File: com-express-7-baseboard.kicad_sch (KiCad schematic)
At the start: 0 parts

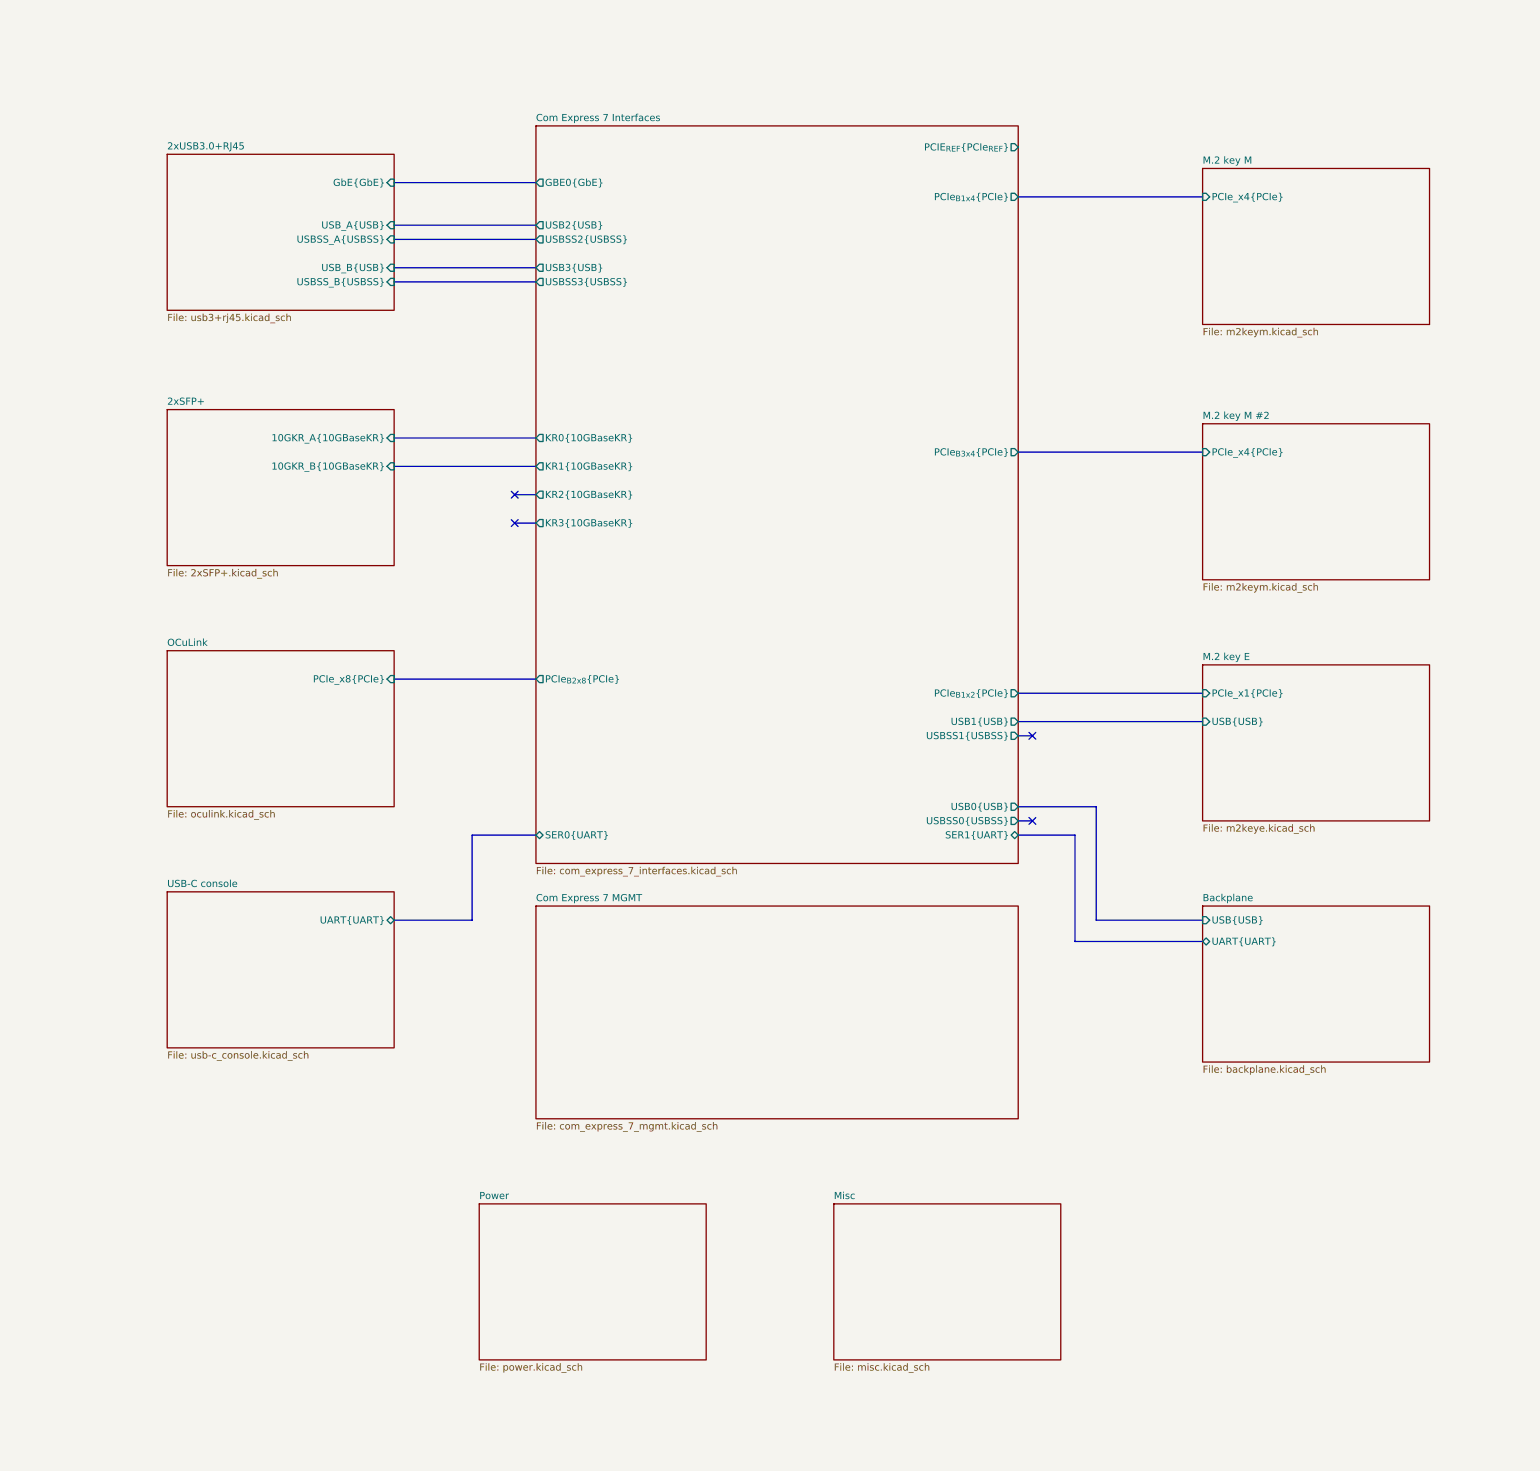
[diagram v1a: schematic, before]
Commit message: [#57056] Create schematics for M.2 and OCuLink connectors
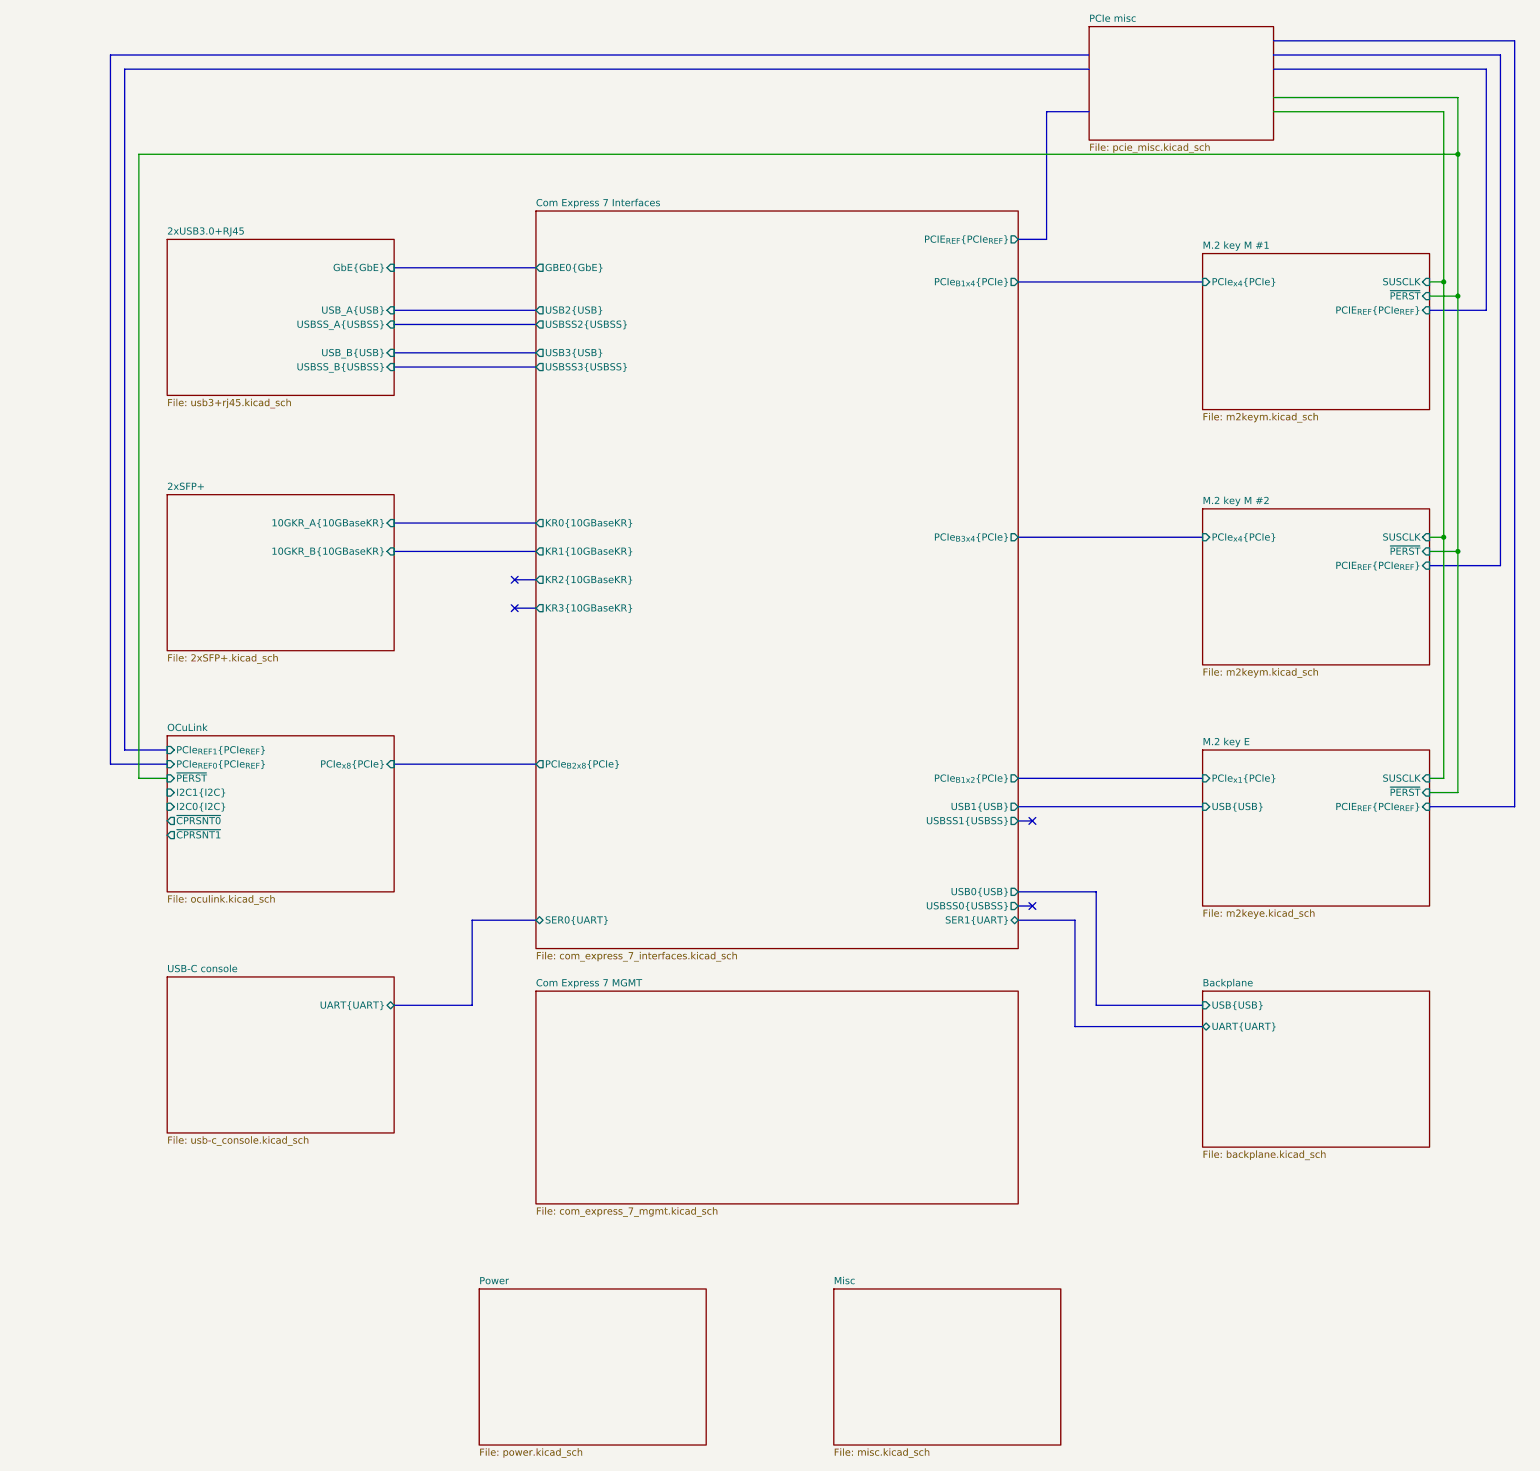
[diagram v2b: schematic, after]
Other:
- sheet M.2 key M renamed M.2 key M #1
- added sheet PCIe misc (pcie_misc.kicad_sch)
- sheet M.2 key E ports: added PCIE_{REF}{PCIe_{REF}}, PCIe_{x1}{PCIe}, SUSCLK, ~{PERST}; removed PCIe_x1{PCIe}
- sheet M.2 key M #1 ports: added PCIE_{REF}{PCIe_{REF}}, PCIe_{x4}{PCIe}, SUSCLK, ~{PERST}; removed PCIe_x4{PCIe}
- sheet M.2 key M #2 ports: added PCIE_{REF}{PCIe_{REF}}, PCIe_{x4}{PCIe}, SUSCLK, ~{PERST}; removed PCIe_x4{PCIe}
- sheet OCuLink ports: added I2C0{I2C}, I2C1{I2C}, PCIe_{REF0}{PCIe_{REF}}, PCIe_{REF1}{PCIe_{REF}}, PCIe_{x8}{PCIe}, ~{CPRSNT0}, ~{CPRSNT1}, ~{PERST}; removed PCIe_x8{PCIe}

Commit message: [#57056] Add PCIe circuitry
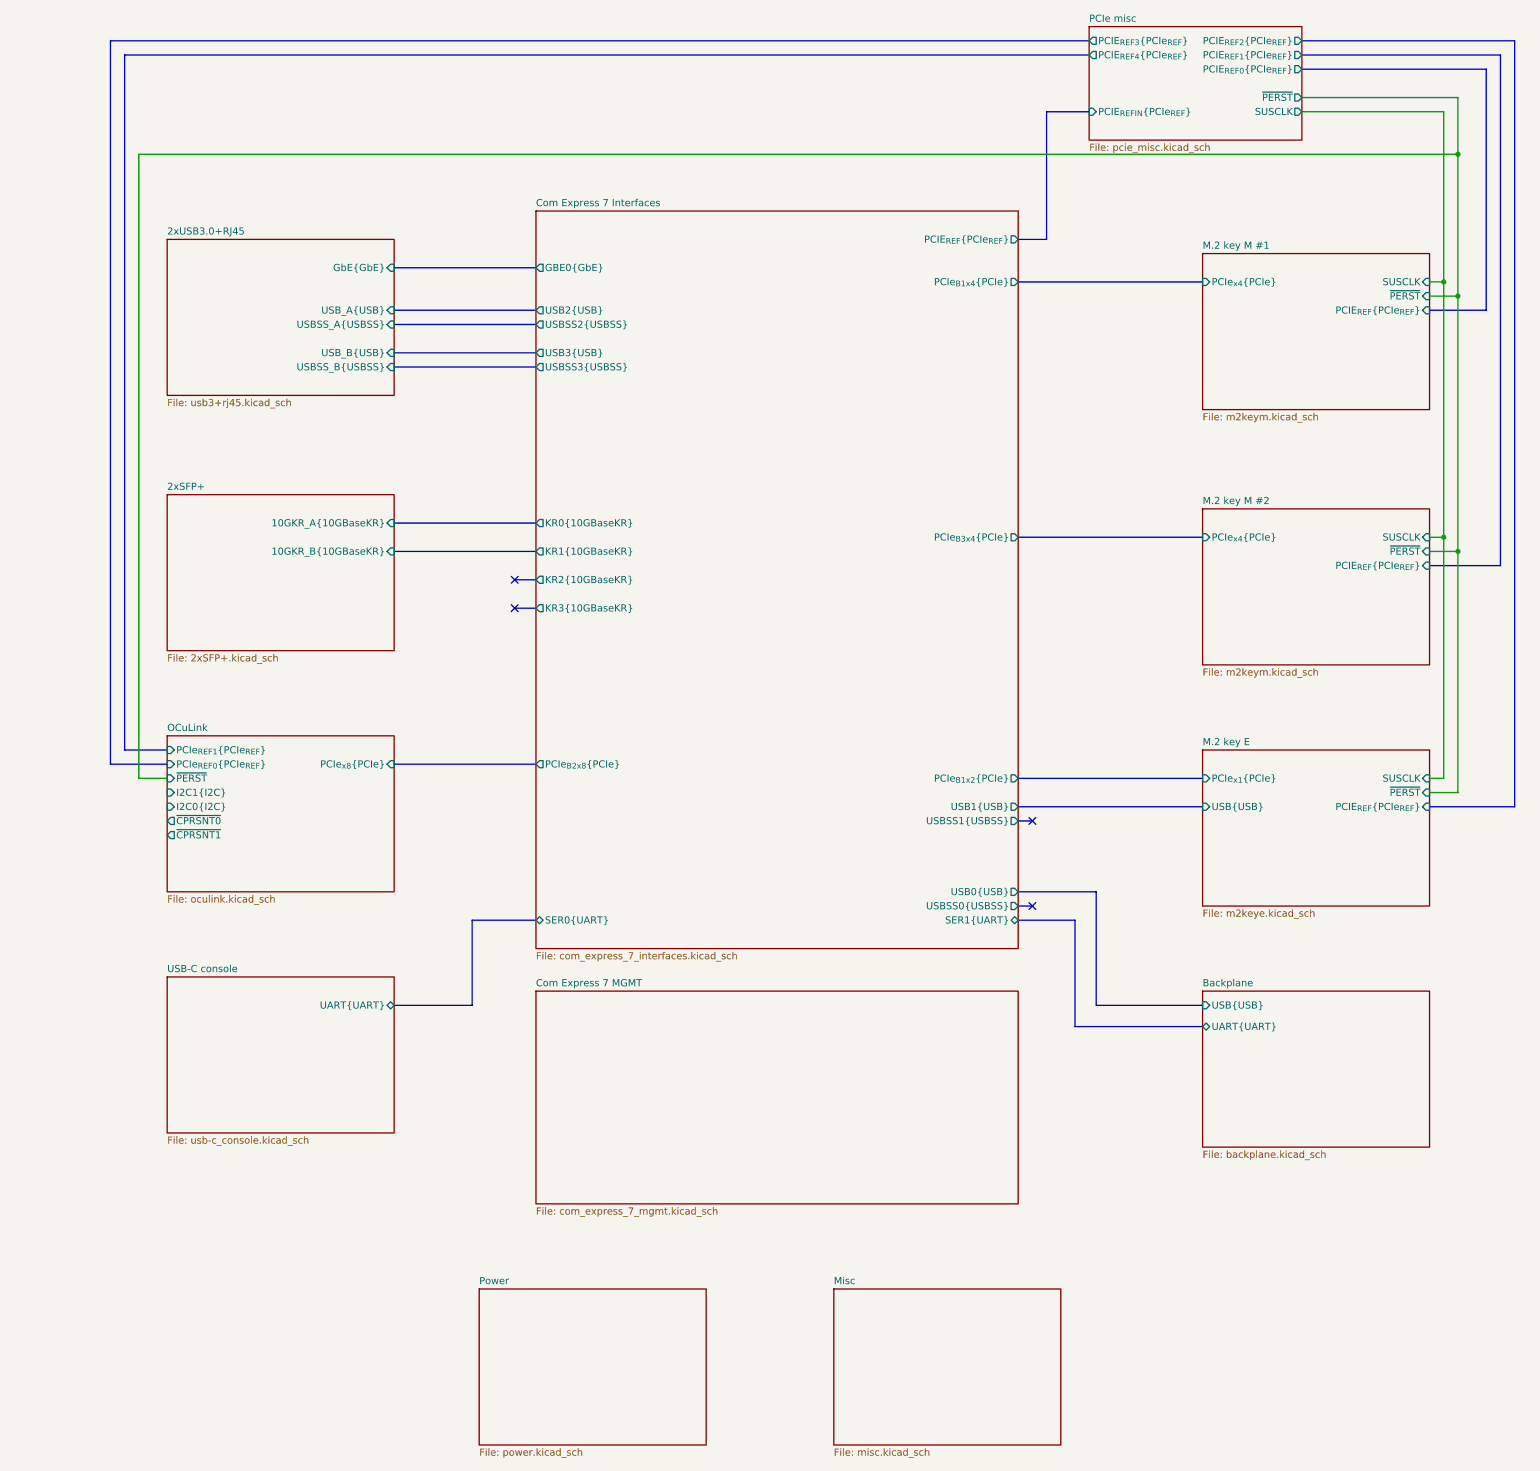
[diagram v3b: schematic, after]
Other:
- sheet PCIe misc ports: added PCIE_{REF0}{PCIe_{REF}}, PCIE_{REF1}{PCIe_{REF}}, PCIE_{REF2}{PCIe_{REF}}, PCIE_{REF3}{PCIe_{REF}}, PCIE_{REF4}{PCIe_{REF}}, PCIE_{REFIN}{PCIe_{REF}}, SUSCLK, ~{PERST}; removed none
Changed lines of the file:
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@@
     (stroke (width 0) (type default) (color 255 153 0 1))
+  )
+  (bus (pts (xy 299.72 25.4) (xy 335.28 25.4))
+    (stroke (width 0) (type default))
   )
   (wire (pts (xy 325.12 66.04) (xy 322.58 66.04))
@@
     (stroke (width 0) (type default))
   )
+  (wire (pts (xy 299.72 33.02) (xy 327.66 33.02))
+    (stroke (width 0) (type default))
+  )
   (bus (pts (xy 262.89 195.58) (xy 281.94 195.58))
     (stroke (width 0) (type default) (color 0 0 255 1))
@@
   )
   (bus (pts (xy 96.52 149.86) (xy 88.9 149.86))
-    (stroke (width 0) (type default))
-  )
-  (bus (pts (xy 294.64 22.86) (xy 337.82 22.86))
     (stroke (width 0) (type default))
   )
@@
     (stroke (width 0) (type default) (color 255 153 0 1))
   )
-  (bus (pts (xy 294.64 25.4) (xy 335.28 25.4))
-    (stroke (width 0) (type default))
-  )
-  (bus (pts (xy 88.9 27.94) (xy 261.62 27.94))
+  (bus (pts (xy 88.9 25.4) (xy 261.62 25.4))
     (stroke (width 0) (type default))
   )
   (bus (pts (xy 259.08 180.34) (xy 259.08 199.39))
     (stroke (width 0) (type default) (color 255 153 0 1))
+  )
+  (bus (pts (xy 299.72 27.94) (xy 332.74 27.94))
+    (stroke (width 0) (type default))
   )
   (bus (pts (xy 158.75 119.38) (xy 162.56 119.38))
@@
     (stroke (width 0) (type default) (color 194 0 194 1))
   )
+  (wire (pts (xy 299.72 35.56) (xy 325.12 35.56))
+    (stroke (width 0) (type default))
+  )
   (wire (pts (xy 322.58 111.76) (xy 325.12 111.76))
     (stroke (width 0) (type default))
   )
-  (bus (pts (xy 86.36 152.4) (xy 86.36 25.4))
+  (bus (pts (xy 86.36 152.4) (xy 86.36 22.86))
     (stroke (width 0) (type default))
   )
@@
     (stroke (width 0) (type default) (color 255 153 0 1))
   )
+  (bus (pts (xy 299.72 22.86) (xy 337.82 22.86))
+    (stroke (width 0) (type default))
+  )
   (bus (pts (xy 137.16 152.4) (xy 162.56 152.4))
     (stroke (width 0) (type default) (color 194 0 194 1))
@@
     (stroke (width 0) (type default) (color 255 0 0 1))
   )
-  (bus (pts (xy 86.36 25.4) (xy 261.62 25.4))
+  (bus (pts (xy 86.36 22.86) (xy 261.62 22.86))
     (stroke (width 0) (type default))
   )
@@
     (stroke (width 0) (type default))
   )
-  (wire (pts (xy 294.64 35.56) (xy 325.12 35.56))
-    (stroke (width 0) (type default))
-  )
-  (wire (pts (xy 294.64 33.02) (xy 327.66 33.02))
-    (stroke (width 0) (type default))
-  )
   (bus (pts (xy 248.92 154.94) (xy 281.94 154.94))
     (stroke (width 0) (type default) (color 194 0 194 1))
   )
-  (bus (pts (xy 294.64 27.94) (xy 332.74 27.94))
-    (stroke (width 0) (type default))
-  )
   (wire (pts (xy 327.66 43.18) (xy 327.66 33.02))
     (stroke (width 0) (type default))
   )
-  (bus (pts (xy 88.9 149.86) (xy 88.9 27.94))
+  (bus (pts (xy 88.9 149.86) (xy 88.9 25.4))
     (stroke (width 0) (type default))
   )
@@
     (stroke (width 0) (type default) (color 0 0 255 1))
   )
-  (sheet (at 261.62 20.32) (size 33.02 20.32) (fields_autoplaced)
+  (sheet (at 261.62 20.32) (size 38.1 20.32) (fields_autoplaced)
     (stroke (width 0.1524) (type solid))
     (fill (color 0 0 0 0.0000))
@@
       (effects (font (size 1.27 1.27)) (justify left top))
     )
+    (pin "PCIE_{REF2}{PCIe_{REF}}" output (at 299.72 22.86 0)
+      (effects (font (size 1.27 1.27)) (justify right))
+    )
+    (pin "PCIE_{REF4}{PCIe_{REF}}" output (at 261.62 25.4 180)
+      (effects (font (size 1.27 1.27)) (justify left))
+    )
+    (pin "PCIE_{REF3}{PCIe_{REF}}" output (at 261.62 22.86 180)
+      (effects (font (size 1.27 1.27)) (justify left))
+    )
+    (pin "PCIE_{REF0}{PCIe_{REF}}" output (at 299.72 27.94 0)
+      (effects (font (size 1.27 1.27)) (justify right))
+    )
+    (pin "PCIE_{REF1}{PCIe_{REF}}" output (at 299.72 25.4 0)
+      (effects (font (size 1.27 1.27)) (justify right))
+    )
+    (pin "PCIE_{REFIN}{PCIe_{REF}}" input (at 261.62 35.56 180)
+      (effects (font (size 1.27 1.27)) (justify left))
+    )
+    (pin "~{PERST}" output (at 299.72 33.02 0)
+      (effects (font (size 1.27 1.27)) (justify right))
+    )
+    (pin "SUSCLK" output (at 299.72 35.56 0)
+      (effects (font (size 1.27 1.27)) (justify right))
+    )
     (instances

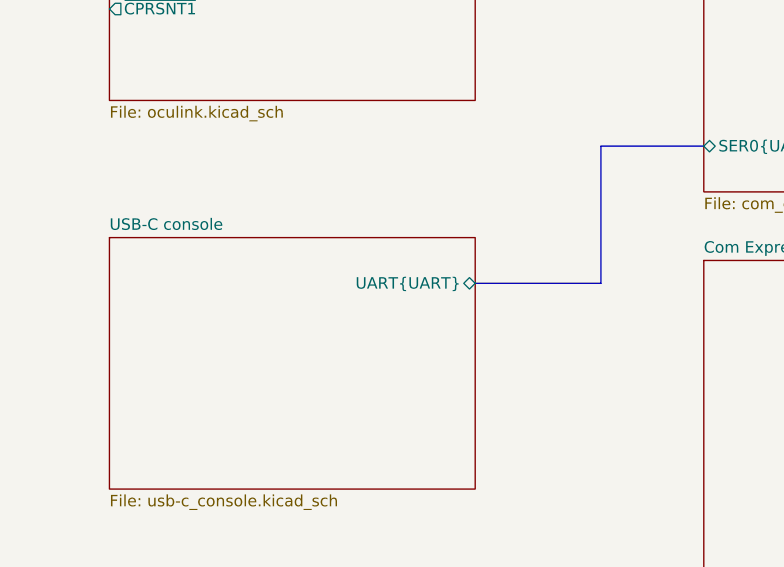
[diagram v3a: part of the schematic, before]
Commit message: [#57056] Add USB-C console
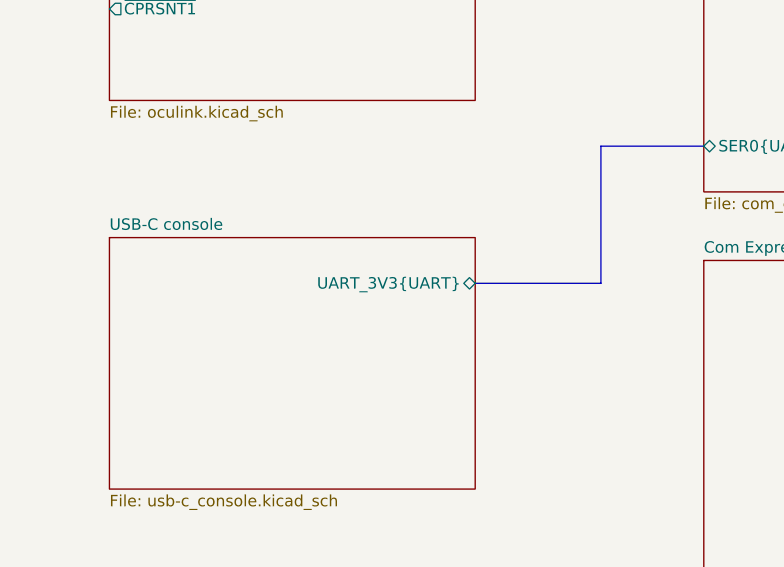
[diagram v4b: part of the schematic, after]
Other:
- sheet USB-C console ports: added UART_3V3{UART}; removed UART{UART}
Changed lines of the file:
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@@
       (effects (font (size 1.27 1.27)) (justify left top))
     )
-    (pin "UART{UART}" bidirectional (at 137.16 195.58 0)
+    (pin "UART_3V3{UART}" bidirectional (at 137.16 195.58 0)
       (effects (font (size 1.27 1.27)) (justify right))
     )
